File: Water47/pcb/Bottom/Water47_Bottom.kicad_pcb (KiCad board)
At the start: 2 copper layers, 260 x 76.5 mm, 8 parts, among them U1 MOUDLE-SEEEDUINO-XIAO

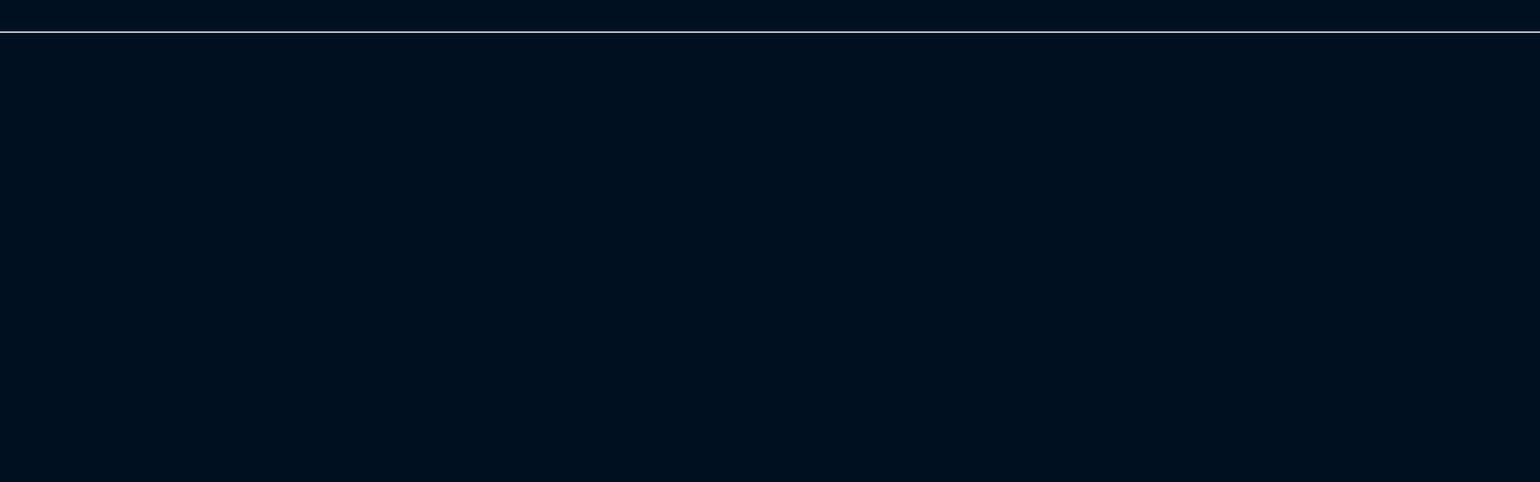
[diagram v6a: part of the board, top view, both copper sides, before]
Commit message: feat: add mounting hole, set gerber path
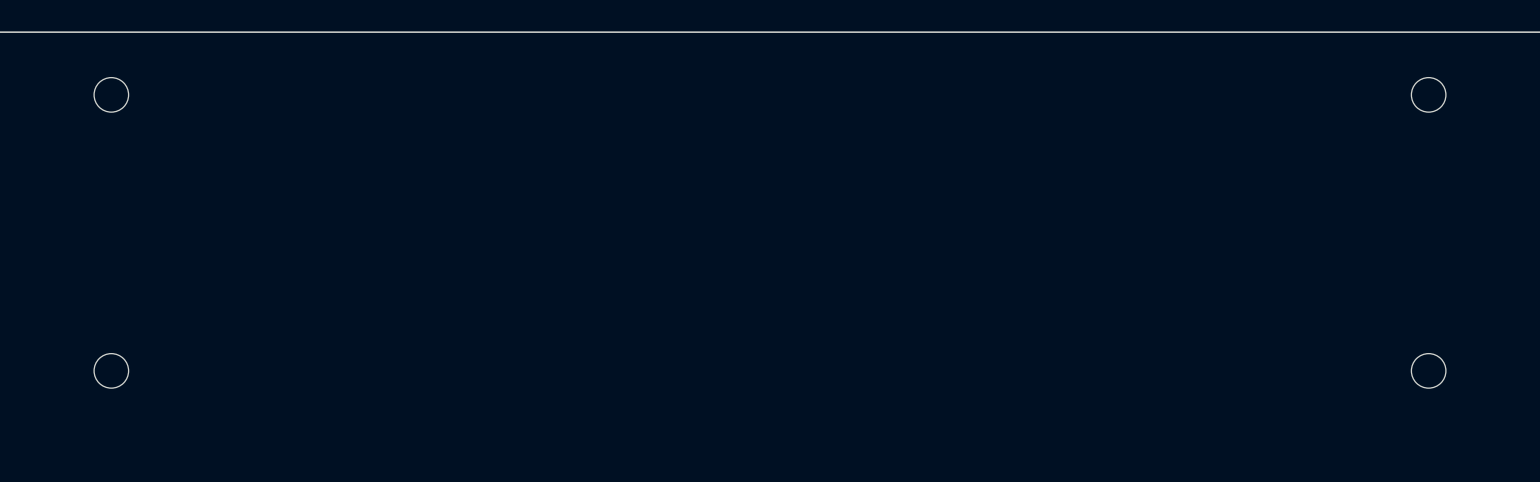
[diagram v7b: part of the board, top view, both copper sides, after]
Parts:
- added H10: MountingHole, kbd_Hole:m2_Screw_Hole, F.Cu at (339.0, 155.7)
- added H7: MountingHole, kbd_Hole:m2_Screw_Hole, F.Cu at (85.0, 155.7)
- added H8: MountingHole, kbd_Hole:m2_Screw_Hole, F.Cu at (339.0, 104.8)
- added H9: MountingHole, kbd_Hole:m2_Screw_Hole, F.Cu at (254.0, 104.8)
- moved H3 182.4 mm to (254.0, 87.2)
- moved H2 169.0 mm to (170.0, 87.2)
- moved H6 169.0 mm to (170.0, 104.8)
- moved H4 68.5 mm to (339.0, 87.2)
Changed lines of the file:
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@@
       (drillshape 0)
       (scaleselection 1)
-      (outputdirectory "../../gerber/PCB_Layer1/")
+      (outputdirectory "../../gerber/03Bottom/")
     )
   )
@@
   (net 13 "+5V")
   (net 14 "unconnected-(U1-Pad2)")
+  (footprint "kbd_Hole:m2_Screw_Hole" (layer "F.Cu")
+    (at 85 155.7)
+    (descr "Mounting Hole 2.2mm, no annular, M2")
+    (tags "mounting hole 2.2mm no annular m2")
+    (property "Sheetfile" "Water47_Bottom.kicad_sch")
+    (property "Sheetname" "")
+    (attr exclude_from_pos_files)
+    (fp_text reference "H7" (at 0 -3.2) (layer "F.Fab")
+      (effects (font (size 1 1) (thickness 0.15)))
+    )
+    (fp_text value "MountingHole" (at 0 3.2) (layer "F.Fab")
+      (effects (font (size 1 1) (thickness 0.15)))
+    )
+    (fp_text user "${REFERENCE}" (at 0.3 0) (layer "F.Fab")
+      (effects (font (size 1 1) (thickness 0.15)))
+    )
+    (fp_circle (center 0 0) (end 2.2 0) (layer "Cmts.User") (width 0.15) (fill none))
+    (fp_circle (center 0 0) (end 2.45 0) (layer "F.CrtYd") (width 0.05) (fill none))
+    (pad "" np_thru_hole circle locked (at 0 0) (size 2.2 2.2) (drill 2.2) (layers *.Cu *.Mask))
+  )
+  (footprint "kbd_Hole:m2_Screw_Hole" (layer "F.Cu")
+    (at 254 104.8)
+    (descr "Mounting Hole 2.2mm, no annular, M2")
+    (tags "mounting hole 2.2mm no annular m2")
+    (property "Sheetfile" "Water47_Bottom.kicad_sch")
+    (property "Sheetname" "")
+    (attr exclude_from_pos_files)
+    (fp_text reference "H9" (at 0 -3.2) (layer "F.Fab")
+      (effects (font (size 1 1) (thickness 0.15)))
+    )
+    (fp_text value "MountingHole" (at 0 3.2) (layer "F.Fab")
+      (effects (font (size 1 1) (thickness 0.15)))
+    )
+    (fp_text user "${REFERENCE}" (at 0.3 0) (layer "F.Fab")
+      (effects (font (size 1 1) (thickness 0.15)))
+    )
+    (fp_circle (center 0 0) (end 2.2 0) (layer "Cmts.User") (width 0.15) (fill none))
+    (fp_circle (center 0 0) (end 2.45 0) (layer "F.CrtYd") (width 0.05) (fill none))
+    (pad "" np_thru_hole circle locked (at 0 0) (size 2.2 2.2) (drill 2.2) (layers *.Cu *.Mask))
+  )
+  (footprint "kbd_Hole:m2_Screw_Hole" (layer "F.Cu")
+    (at 339 155.7)
+    (descr "Mounting Hole 2.2mm, no annular, M2")
+    (tags "mounting hole 2.2mm no annular m2")
+    (property "Sheetfile" "Water47_Bottom.kicad_sch")
+    (property "Sheetname" "")
+    (attr exclude_from_pos_files)
+    (fp_text reference "H10" (at 0 -3.2) (layer "F.Fab")
+      (effects (font (size 1 1) (thickness 0.15)))
+    )
+    (fp_text value "MountingHole" (at 0 3.2) (layer "F.Fab")
+      (effects (font (size 1 1) (thickness 0.15)))
+    )
+    (fp_text user "${REFERENCE}" (at 0.3 0) (layer "F.Fab")
+      (effects (font (size 1 1) (thickness 0.15)))
+    )
+    (fp_circle (center 0 0) (end 2.2 0) (layer "Cmts.User") (width 0.15) (fill none))
+    (fp_circle (center 0 0) (end 2.45 0) (layer "F.CrtYd") (width 0.05) (fill none))
+    (pad "" np_thru_hole circle locked (at 0 0) (size 2.2 2.2) (drill 2.2) (layers *.Cu *.Mask))
+  )
   (footprint "kbd_Parts:Micon_XIAO_TH" (layer "F.Cu")
     (at 326.23125 95.5)
@@
   )
   (footprint "kbd_Hole:m2_Screw_Hole" (layer "F.Cu")
+    (at 170 87.2)
+    (descr "Mounting Hole 2.2mm, no annular, M2")
+    (tags "mounting hole 2.2mm no annular m2")
+    (property "Sheetfile" "Water47_Bottom.kicad_sch")
+    (property "Sheetname" "")
+    (attr exclude_from_pos_files)
+    (fp_text reference "H2" (at 0 -3.2) (layer "F.Fab")
+      (effects (font (size 1 1) (thickness 0.15)))
+    )
+    (fp_text value "MountingHole" (at 0 3.2) (layer "F.Fab")
+      (effects (font (size 1 1) (thickness 0.15)))
+    )
+    (fp_text user "${REFERENCE}" (at 0.3 0) (layer "F.Fab")
+      (effects (font (size 1 1) (thickness 0.15)))
+    )
+    (fp_circle (center 0 0) (end 2.2 0) (layer "Cmts.User") (width 0.15) (fill none))
+    (fp_circle (center 0 0) (end 2.45 0) (layer "F.CrtYd") (width 0.05) (fill none))
+    (pad "" np_thru_hole circle locked (at 0 0) (size 2.2 2.2) (drill 2.2) (layers *.Cu *.Mask))
+  )
+  (footprint "kbd_Hole:m2_Screw_Hole" (layer "F.Cu")
+    (at 170 104.8)
+    (descr "Mounting Hole 2.2mm, no annular, M2")
+    (tags "mounting hole 2.2mm no annular m2")
+    (property "Sheetfile" "Water47_Bottom.kicad_sch")
+    (property "Sheetname" "")
+    (attr exclude_from_pos_files)
+    (fp_text reference "H6" (at 0 -3.2) (layer "F.Fab")
+      (effects (font (size 1 1) (thickness 0.15)))
+    )
+    (fp_text value "MountingHole" (at 0 3.2) (layer "F.Fab")
+      (effects (font (size 1 1) (thickness 0.15)))
+    )
+    (fp_text user "${REFERENCE}" (at 0.3 0) (layer "F.Fab")
+      (effects (font (size 1 1) (thickness 0.15)))
+    )
+    (fp_circle (center 0 0) (end 2.2 0) (layer "Cmts.User") (width 0.15) (fill none))
+    (fp_circle (center 0 0) (end 2.45 0) (layer "F.CrtYd") (width 0.05) (fill none))
+    (pad "" np_thru_hole circle locked (at 0 0) (size 2.2 2.2) (drill 2.2) (layers *.Cu *.Mask))
+  )
+  (footprint "kbd_Hole:m2_Screw_Hole" (layer "F.Cu")
     (at 339 87.2)
     (descr "Mounting Hole 2.2mm, no annular, M2")
@@
     (property "Sheetname" "")
     (attr exclude_from_pos_files)
-    (fp_text reference "H2" (at 0 -3.2) (layer "F.Fab")
+    (fp_text reference "H4" (at 0 -3.2) (layer "F.Fab")
       (effects (font (size 1 1) (thickness 0.15)))
     )
@@
     (property "Sheetname" "")
     (attr exclude_from_pos_files)
-    (fp_text reference "H6" (at 0 -3.2) (layer "F.Fab")
-      (effects (font (size 1 1) (thickness 0.15)))
-    )
-    (fp_text value "MountingHole" (at 0 3.2) (layer "F.Fab")
-      (effects (font (size 1 1) (thickness 0.15)))
-    )
-    (fp_text user "${REFERENCE}" (at 0.3 0) (layer "F.Fab")
-      (effects (font (size 1 1) (thickness 0.15)))
-    )
-    (fp_circle (center 0 0) (end 2.2 0) (layer "Cmts.User") (width 0.15) (fill none))
-    (fp_circle (center 0 0) (end 2.45 0) (layer "F.CrtYd") (width 0.05) (fill none))
-    (pad "" np_thru_hole circle locked (at 0 0) (size 2.2 2.2) (drill 2.2) (layers *.Cu *.Mask))
-  )
-  (footprint "kbd_Hole:m2_Screw_Hole" (layer "F.Cu")
-    (at 339 155.7)
-    (descr "Mounting Hole 2.2mm, no annular, M2")
-    (tags "mounting hole 2.2mm no annular m2")
-    (property "Sheetfile" "Water47_Bottom.kicad_sch")
-    (property "Sheetname" "")
-    (attr exclude_from_pos_files)
-    (fp_text reference "H4" (at 0 -3.2) (layer "F.Fab")
-      (effects (font (size 1 1) (thickness 0.15)))
-    )
-    (fp_text value "MountingHole" (at 0 3.2) (layer "F.Fab")
-      (effects (font (size 1 1) (thickness 0.15)))
-    )
-    (fp_text user "${REFERENCE}" (at 0.3 0) (layer "F.Fab")
-      (effects (font (size 1 1) (thickness 0.15)))
-    )
-    (fp_circle (center 0 0) (end 2.2 0) (layer "Cmts.User") (width 0.15) (fill none))
-    (fp_circle (center 0 0) (end 2.45 0) (layer "F.CrtYd") (width 0.05) (fill none))
-    (pad "" np_thru_hole circle locked (at 0 0) (size 2.2 2.2) (drill 2.2) (layers *.Cu *.Mask))
-  )
-  (footprint "kbd_Hole:m2_Screw_Hole" (layer "F.Cu")
-    (at 85 155.7)
-    (descr "Mounting Hole 2.2mm, no annular, M2")
-    (tags "mounting hole 2.2mm no annular m2")
+    (fp_text reference "H8" (at 0 -3.2) (layer "F.Fab")
+      (effects (font (size 1 1) (thickness 0.15)))
+    )
+    (fp_text value "MountingHole" (at 0 3.2) (layer "F.Fab")
+      (effects (font (size 1 1) (thickness 0.15)))
+    )
+    (fp_text user "${REFERENCE}" (at 0.3 0) (layer "F.Fab")
+      (effects (font (size 1 1) (thickness 0.15)))
+    )
+    (fp_circle (center 0 0) (end 2.2 0) (layer "Cmts.User") (width 0.15) (fill none))
+    (fp_circle (center 0 0) (end 2.45 0) (layer "F.CrtYd") (width 0.05) (fill none))
+    (pad "" np_thru_hole circle locked (at 0 0) (size 2.2 2.2) (drill 2.2) (layers *.Cu *.Mask))
+  )
+  (footprint "kbd_Hole:m2_Screw_Hole" (layer "F.Cu")
+    (at 254 87.2)
+    (descr "Mounting Hole 2.2mm, no annular, M2")
+    (tags "mounting hole 2.2mm no annular m2")

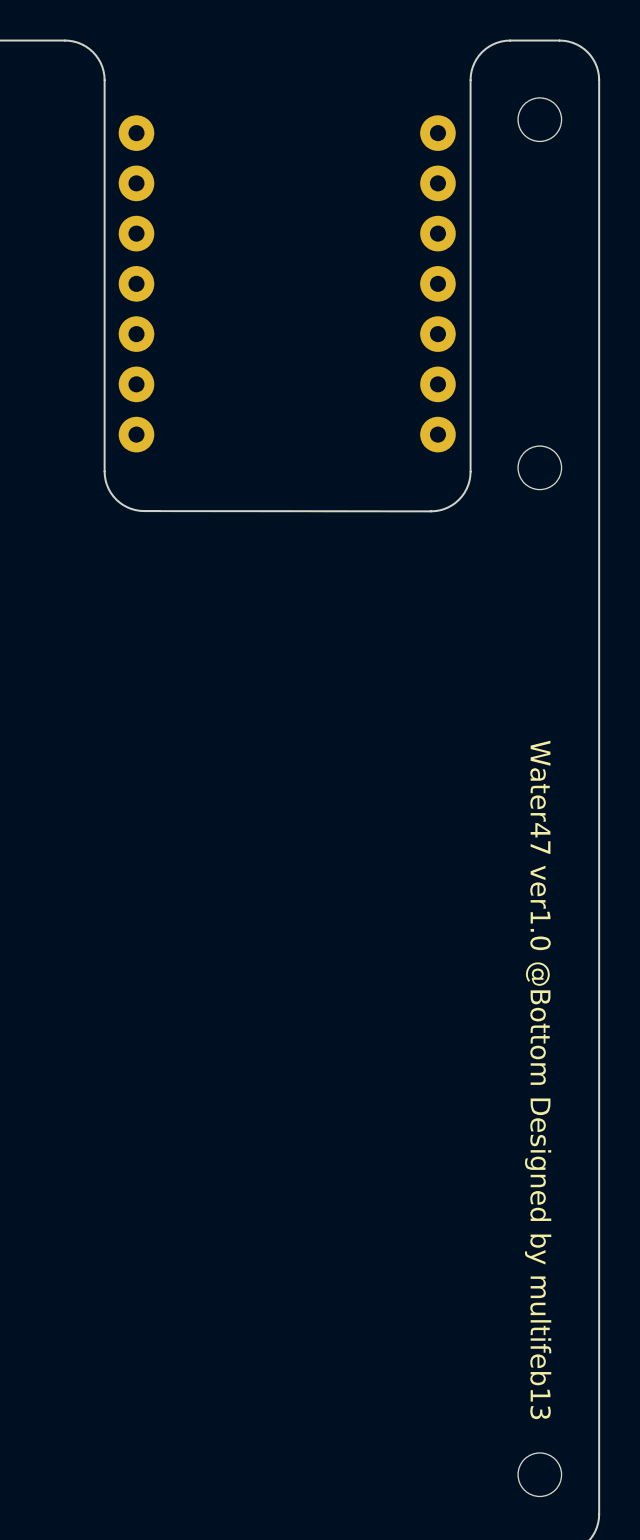
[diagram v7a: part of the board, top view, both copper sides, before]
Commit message: feat: remove unused micon footprint
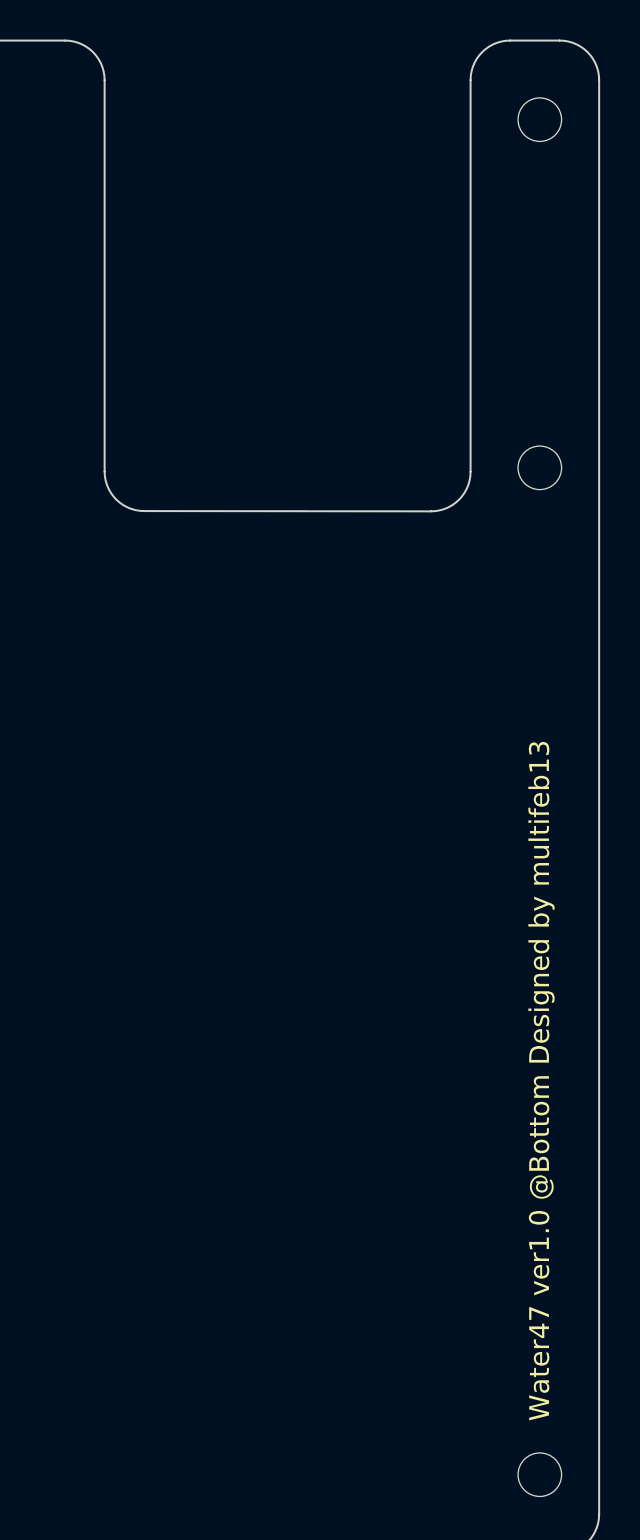
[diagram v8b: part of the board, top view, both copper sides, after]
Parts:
- removed U1: MOUDLE-SEEEDUINO-XIAO, kbd_Parts:Micon_XIAO_TH
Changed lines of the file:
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@@
   )
   (net 0 "")
-  (net 1 "PIN1")
-  (net 2 "PIN2")
-  (net 3 "PIN3")
-  (net 4 "PIN4")
-  (net 5 "PIN5")
-  (net 6 "PIN6")
-  (net 7 "PIN7")
-  (net 8 "PIN8")
-  (net 9 "SDA")
-  (net 10 "SCL")
-  (net 11 "+3.3V")
-  (net 12 "GND")
-  (net 13 "+5V")
-  (net 14 "unconnected-(U1-Pad2)")
   (footprint "kbd_Hole:m2_Screw_Hole" (layer "F.Cu")
     (at 85 155.7)
@@
     (pad "" np_thru_hole circle locked (at 0 0) (size 2.2 2.2) (drill 2.2) (layers *.Cu *.Mask))
   )
-  (footprint "kbd_Parts:Micon_XIAO_TH" (layer "F.Cu")
-    (at 326.23125 95.5)
-    (property "Datasheet_1" "")
-    (property "Footprint_1" "")
-    (property "Reference_1" "U1")
-    (property "Sheetfile" "Water47_Bottom.kicad_sch")
-    (property "Sheetname" "")
-    (property "Value_1" "MOUDLE-SEEEDUINO-XIAO")
-    (attr smd board_only exclude_from_pos_files)
-    (fp_text reference "U1" (at 0 -2.25) (layer "F.SilkS") hide
-      (effects (font (size 0.889 0.889) (thickness 0.1016)))
-    )
-    (fp_text value "MOUDLE-SEEEDUINO-XIAO" (at 0 -3.275) (layer "B.SilkS")
-      (effects (font (size 0.6096 0.6096) (thickness 0.0762)) (justify mirror))
-    )
-    (fp_rect (start 3.350197 -6.785813) (end 5.128197 -4.118813) (layer "Dwgs.User") (width 0.12) (fill none))
-    (fp_rect (start 3.350197 -10.849813) (end 5.128197 -8.182813) (layer "Dwgs.User") (width 0.12) (fill none))
-    (fp_rect (start -3.507811 -8.182813) (end -5.285811 -10.849813) (layer "Dwgs.User") (width 0.12) (fill none))
-    (fp_rect (start -8.89 10.5) (end 8.89 -10.5) (layer "Dwgs.User") (width 0.12) (fill none))
-    (fp_rect (start -5.285811 -6.785813) (end -3.507811 -4.118813) (layer "Dwgs.User") (width 0.12) (fill none))
-    (fp_rect (start -4.5 -12.15) (end 4.5 -4.65) (layer "Dwgs.User") (width 0.12) (fill none))
-    (pad "1" thru_hole circle (at 7.62 -7.62 180) (size 1.8 1.8) (drill 0.8128) (layers *.Cu *.Mask)
-      (net 1 "PIN1") (pinfunction "PA02_A0_D0") (pintype "passive"))
-    (pad "2" thru_hole circle (at 7.62 -5.08 180) (size 1.8 1.8) (drill 0.8128) (layers *.Cu *.Mask)
-      (net 14 "unconnected-(U1-Pad2)") (pinfunction "PA4_A1_D1") (pintype "passive+no_connect"))
-    (pad "3" thru_hole circle (at 7.62 -2.54 180) (size 1.8 1.8) (drill 0.8128) (layers *.Cu *.Mask)
-      (net 5 "PIN5") (pinfunction "PA10_A2_D2") (pintype "passive"))
-    (pad "4" thru_hole circle (at 7.62 0 180) (size 1.8 1.8) (drill 0.8128) (layers *.Cu *.Mask)
-      (net 3 "PIN3") (pinfunction "PA11_A3_D3") (pintype "passive"))
-    (pad "5" thru_hole circle (at 7.62 2.54 180) (size 1.8 1.8) (drill 0.8128) (layers *.Cu *.Mask)
-      (net 9 "SDA") (pinfunction "PA8_A4_D4_SDA") (pintype "passive"))
-    (pad "6" thru_hole circle (at 7.62 5.08 180) (size 1.8 1.8) (drill 0.8128) (layers *.Cu *.Mask)
-      (net 10 "SCL") (pinfunction "PA9_A5_D5_SCL") (pintype "passive"))
-    (pad "7" thru_hole circle (at 7.62 7.62 180) (size 1.8 1.8) (drill 0.8128) (layers *.Cu *.Mask)
-      (net 8 "PIN8") (pinfunction "PB08_A6_D6_TX") (pintype "passive"))
-    (pad "8" thru_hole circle (at -7.62 7.62) (size 1.8 1.8) (drill 0.8128) (layers *.Cu *.Mask)
-      (net 7 "PIN7") (pinfunction "PB09_A7_D7_RX") (pintype "passive"))
-    (pad "9" thru_hole circle (at -7.62 5.08) (size 1.8 1.8) (drill 0.8128) (layers *.Cu *.Mask)
-      (net 2 "PIN2") (pinfunction "PA7_A8_D8_SCK") (pintype "passive"))
-    (pad "10" thru_hole circle (at -7.62 2.54) (size 1.8 1.8) (drill 0.8128) (layers *.Cu *.Mask)
-      (net 6 "PIN6") (pinfunction "PA5_A9_D9_MISO") (pintype "passive"))
-    (pad "11" thru_hole circle (at -7.62 0) (size 1.8 1.8) (drill 0.8128) (layers *.Cu *.Mask)
-      (net 4 "PIN4") (pinfunction "PA6_A10_D10_MOSI") (pintype "passive"))
-    (pad "12" thru_hole circle (at -7.62 -2.54) (size 1.8 1.8) (drill 0.8128) (layers *.Cu *.Mask)
-      (net 11 "+3.3V") (pinfunction "3V3") (pintype "passive"))
-    (pad "13" thru_hole circle (at -7.62 -5.08) (size 1.8 1.8) (drill 0.8128) (layers *.Cu *.Mask)
-      (net 12 "GND") (pinfunction "GND") (pintype "passive"))
-    (pad "14" thru_hole circle (at -7.62 -7.62) (size 1.8 1.8) (drill 0.8128) (layers *.Cu *.Mask)
-      (net 13 "+5V") (pinfunction "5V") (pintype "passive"))
-  )
   (footprint "kbd_Hole:m2_Screw_Hole" (layer "F.Cu")
     (at 85 87.2)
@@
   (gr_arc (start 319 106.985786) (mid 317.585786 106.4) (end 317 104.985786) (layer "Edge.Cuts") (width 0.1))
   (gr_arc (start 84 159.7) (mid 82.585786 159.114214) (end 82 157.7) (layer "Edge.Cuts") (width 0.1))
-  (gr_text "Water47 ver1.0 @Bottom Designed by multifeb13" (at 339 153 -90) (layer "F.SilkS")
-    (effects (font (size 1 1) (thickness 0.125)) (justify right))
+  (gr_text "Water47 ver1.0 @Bottom Designed by multifeb13" (at 339 153 90) (layer "F.SilkS")
+    (effects (font (size 1 1) (thickness 0.125)) (justify left))
   )
   (dimension (type aligned) (layer "Cmts.User")
